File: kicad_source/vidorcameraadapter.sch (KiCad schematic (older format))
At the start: 44 parts, among them CN1 CONN_02X26, CN2 CONN_02X10, CN3 CONN_01X03

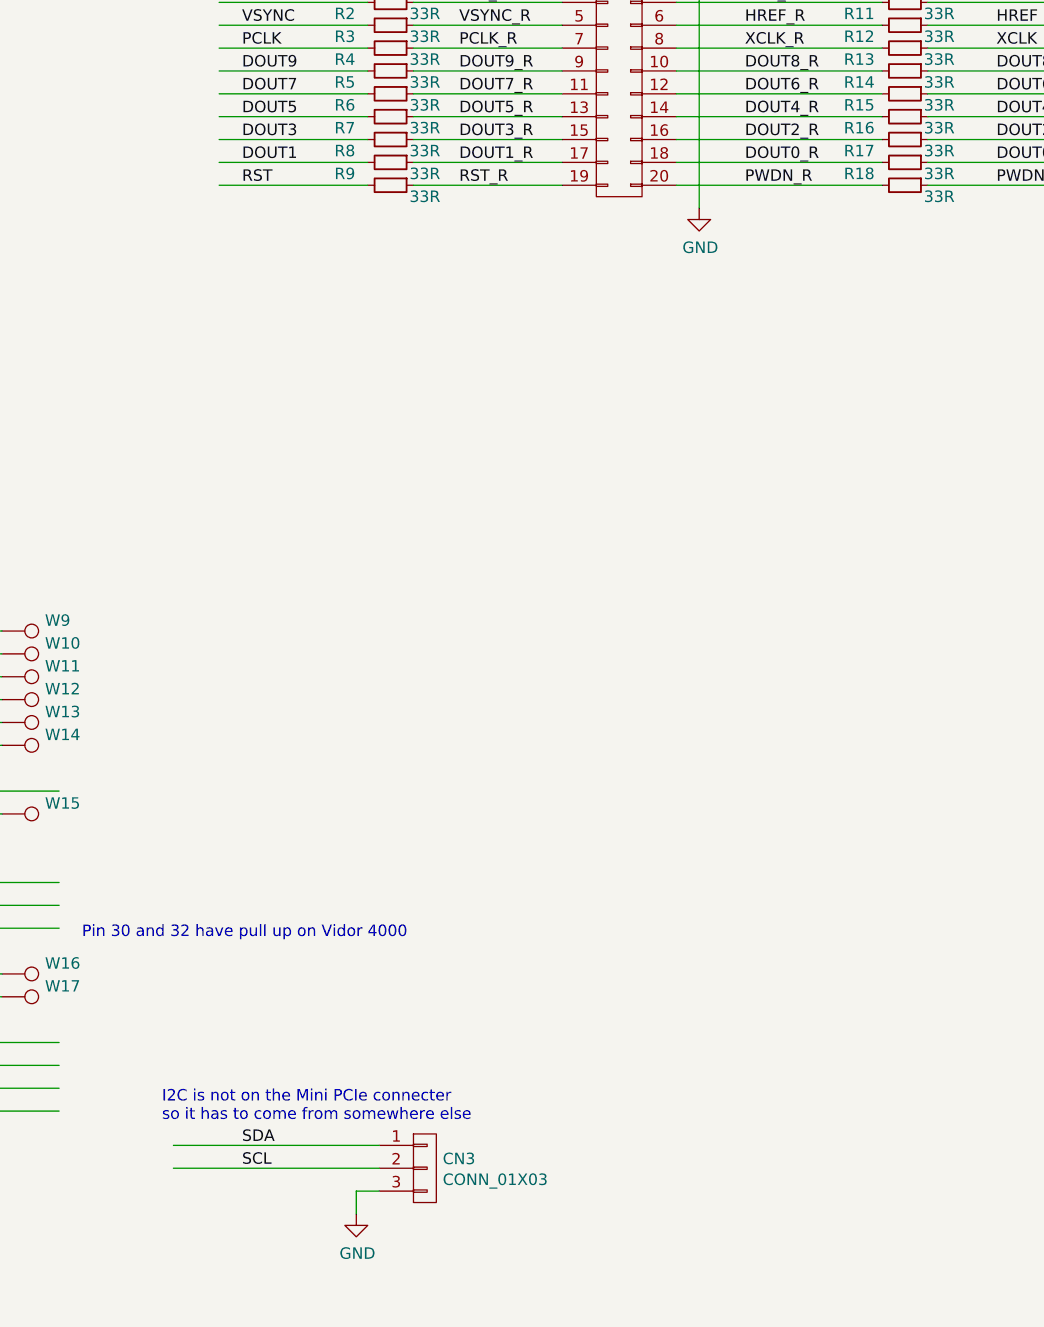
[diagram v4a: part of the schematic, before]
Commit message: added pull up for I2C and RST, added pull down for pwdn
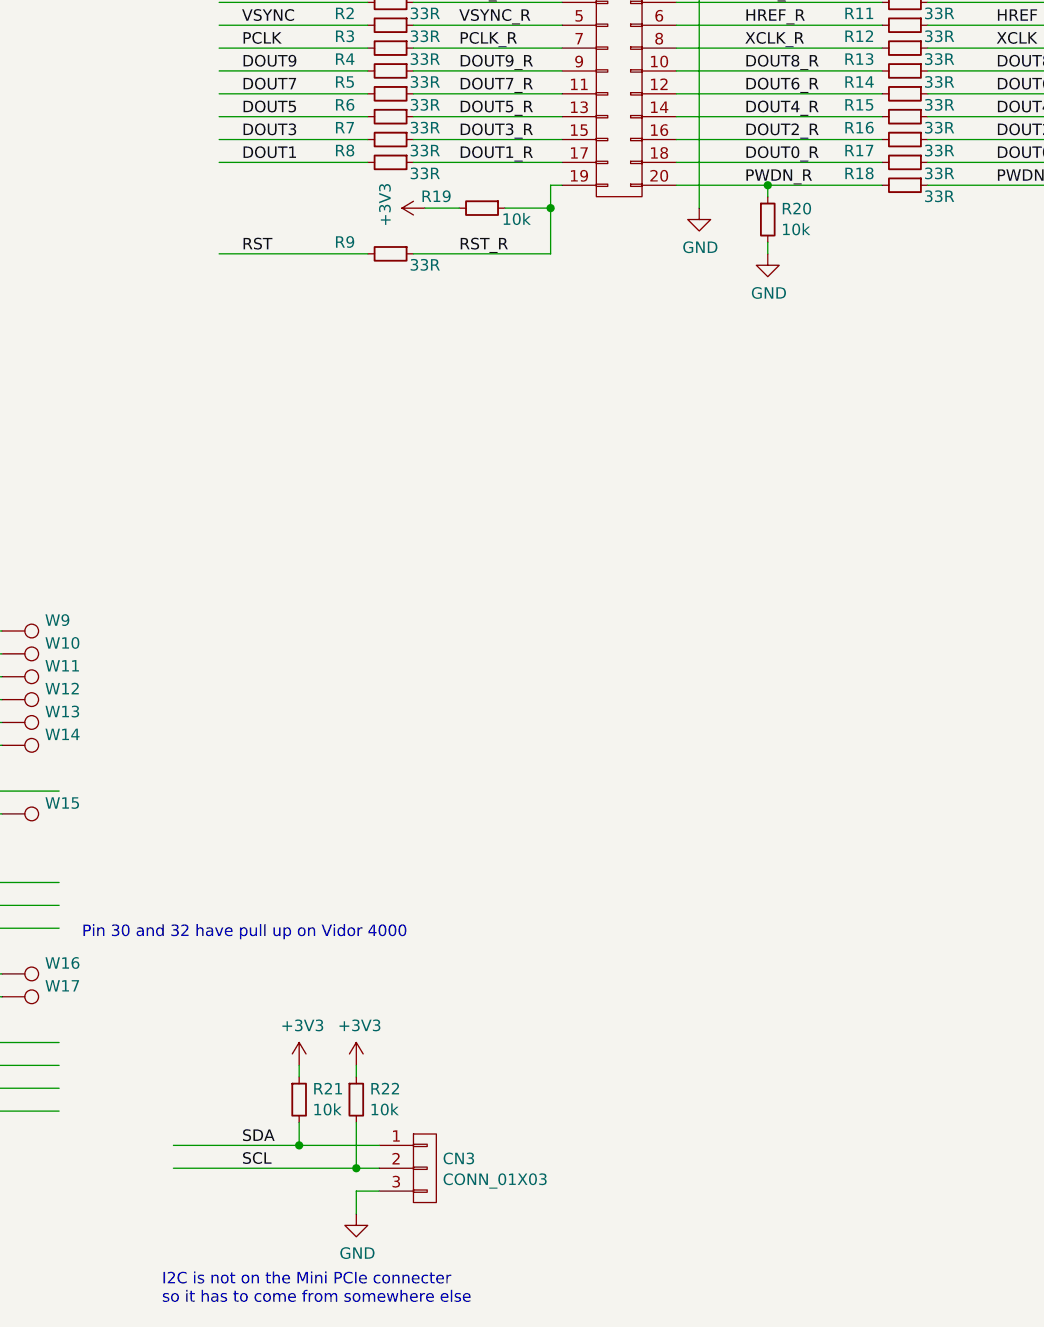
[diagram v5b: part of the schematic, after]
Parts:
- added R19, R20, R21, R22: 10k, resistors:R_0603, symbol devices:R_0603
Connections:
- wire segments 115 -> 129
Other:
- moved on the sheet: R9
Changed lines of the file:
@@
 	6300 2350 6950 2350
 Wire Wire Line
-	6300 2450 6950 2450
-Wire Wire Line
 	8350 1650 7450 1650
 Wire Wire Line
@@
 	8350 2350 7450 2350
 Wire Wire Line
-	8350 2450 7450 2450
+	8350 2450 7850 2450
 Text Label 6500 1650 0    50   ~ 0
 SCL_R
@@
 Text Label 7750 1850 0    50   ~ 0
 XCLK_R
-Text Label 6500 2450 0    50   ~ 0
+Text Label 6500 2750 0    50   ~ 0
 RST_R
 Text Label 7750 2450 0    50   ~ 0
@@
 DOUT1
 Wire Wire Line
-	6150 6650 5250 6650
-Wire Wire Line
-	6150 6750 5250 6750
+	6150 6650 5800 6650
+Wire Wire Line
+	6150 6750 6050 6750
 Text Label 5550 6650 0    50   ~ 0
 SDA
@@
 Wire Wire Line
 	6050 6850 6050 6950
-Text Notes 5200 6550 0    50   ~ 0
+Text Notes 5200 7350 0    50   ~ 0
 I2C is not on the Mini PCIe connecter\nso it has to come from somewhere else
 $Comp
@@
 Wire Wire Line
 	5450 2350 6100 2350
-Wire Wire Line
-	5450 2450 6100 2450
 Text Label 5550 1650 0    50   ~ 0
 SCL
@@
 Text Label 5550 1850 0    50   ~ 0
 PCLK
-Text Label 5550 2450 0    50   ~ 0
+Text Label 5550 2750 0    50   ~ 0
 RST
 Text Label 5550 1950 0    50   ~ 0
@@
 L devices:R_0603 R9
 U 1 1 5E32ABC3
-P 6200 2450
-F 0 "R9" V 6150 2250 50  0000 C CNN
-F 1 "33R" V 6250 2600 50  0000 C CNN
-F 2 "resistors:R_0603" H 6200 2300 50  0001 C CNN
-F 3 "" H 6200 2450 50  0000 C CNN
-	1    6200 2450
+P 6200 2750
+F 0 "R9" V 6150 2550 50  0000 C CNN
+F 1 "33R" V 6250 2900 50  0000 C CNN
+F 2 "resistors:R_0603" H 6200 2600 50  0001 C CNN
+F 3 "" H 6200 2750 50  0000 C CNN
+	1    6200 2750
 	0    1    1    0
 $EndComp
@@
 	0    -1   -1   0
 $EndComp
+Wire Wire Line
+	5450 2750 6100 2750
+Wire Wire Line
+	6300 2750 6900 2750
+Wire Wire Line
+	6900 2750 6900 2550
+Wire Wire Line
+	6900 2450 6950 2450
+$Comp
+L devices:R_0603 R19
+U 1 1 5E34B16D
+P 6600 2550
+F 0 "R19" V 6550 2350 50  0000 C CNN
+F 1 "10k" V 6650 2700 50  0000 C CNN
+F 2 "resistors:R_0603" H 6600 2400 50  0001 C CNN
+F 3 "" H 6600 2550 50  0000 C CNN
+	1    6600 2550
+	0    1    1    0
+$EndComp
+$Comp
+L power-supply:+3V3 #PWR02
+U 1 1 5E34B540
+P 6350 2550
+F 0 "#PWR02" H 6350 2400 50  0001 C CNN
+F 1 "+3V3" H 6365 2723 50  0000 C CNN
+F 2 "" H 6350 2550 50  0000 C CNN
+F 3 "" H 6350 2550 50  0000 C CNN
+	1    6350 2550
+	0    -1   -1   0
+$EndComp
+Wire Wire Line
+	6350 2550 6500 2550
+Wire Wire Line
+	6700 2550 6900 2550
+Connection ~ 6900 2550
+Wire Wire Line
+	6900 2550 6900 2450
+$Comp
+L devices:R_0603 R20
+U 1 1 5E358A18
+P 7850 2600
+F 0 "R20" H 7909 2646 50  0000 L CNN
+F 1 "10k" H 7909 2555 50  0000 L CNN
+F 2 "resistors:R_0603" H 7850 2450 50  0001 C CNN
+F 3 "" H 7850 2600 50  0000 C CNN
+	1    7850 2600
+	1    0    0    -1
+$EndComp
+$Comp
+L power-supply:GND #PWR03
+U 1 1 5E359892
+P 7850 2750
+F 0 "#PWR03" H 7850 2500 50  0001 C CNN
+F 1 "GND" H 7855 2577 50  0000 C CNN
+F 2 "" H 7850 2750 50  0000 C CNN
+F 3 "" H 7850 2750 50  0000 C CNN
+	1    7850 2750
+	1    0    0    -1
+$EndComp
+Wire Wire Line
+	7850 2500 7850 2450
+Connection ~ 7850 2450
+Wire Wire Line
+	7850 2450 7450 2450
+Wire Wire Line
+	7850 2700 7850 2750
+$Comp
+L devices:R_0603 R21
+U 1 1 5E3698B8
+P 5800 6450
+F 0 "R21" H 5859 6496 50  0000 L CNN
+F 1 "10k" H 5859 6405 50  0000 L CNN
+F 2 "resistors:R_0603" H 5800 6300 50  0001 C CNN
+F 3 "" H 5800 6450 50  0000 C CNN
+	1    5800 6450
+	1    0    0    -1
+$EndComp
+$Comp
+L devices:R_0603 R22
+U 1 1 5E36B62F
+P 6050 6450
+F 0 "R22" H 6109 6496 50  0000 L CNN
+F 1 "10k" H 6109 6405 50  0000 L CNN
+F 2 "resistors:R_0603" H 6050 6300 50  0001 C CNN
+F 3 "" H 6050 6450 50  0000 C CNN
+	1    6050 6450
+	1    0    0    -1
+$EndComp
+$Comp
+L power-supply:+3V3 #PWR04
+U 1 1 5E36D8CA
+P 5800 6300
+F 0 "#PWR04" H 5800 6150 50  0001 C CNN
+F 1 "+3V3" H 5815 6473 50  0000 C CNN
+F 2 "" H 5800 6300 50  0000 C CNN
+F 3 "" H 5800 6300 50  0000 C CNN
+	1    5800 6300
+	1    0    0    -1
+$EndComp
+$Comp
+L power-supply:+3V3 #PWR05
+U 1 1 5E370008
+P 6050 6300
+F 0 "#PWR05" H 6050 6150 50  0001 C CNN
+F 1 "+3V3" H 6065 6473 50  0000 C CNN
+F 2 "" H 6050 6300 50  0000 C CNN
+F 3 "" H 6050 6300 50  0000 C CNN
+	1    6050 6300
+	1    0    0    -1
+$EndComp
+Wire Wire Line
+	5800 6550 5800 6650
+Connection ~ 5800 6650
+Wire Wire Line
+	5800 6650 5250 6650
+Wire Wire Line
+	6050 6550 6050 6750
+Connection ~ 6050 6750
+Wire Wire Line
+	6050 6750 5250 6750
+Wire Wire Line
+	6050 6350 6050 6300
+Wire Wire Line
+	5800 6350 5800 6300
 $EndSCHEMATC

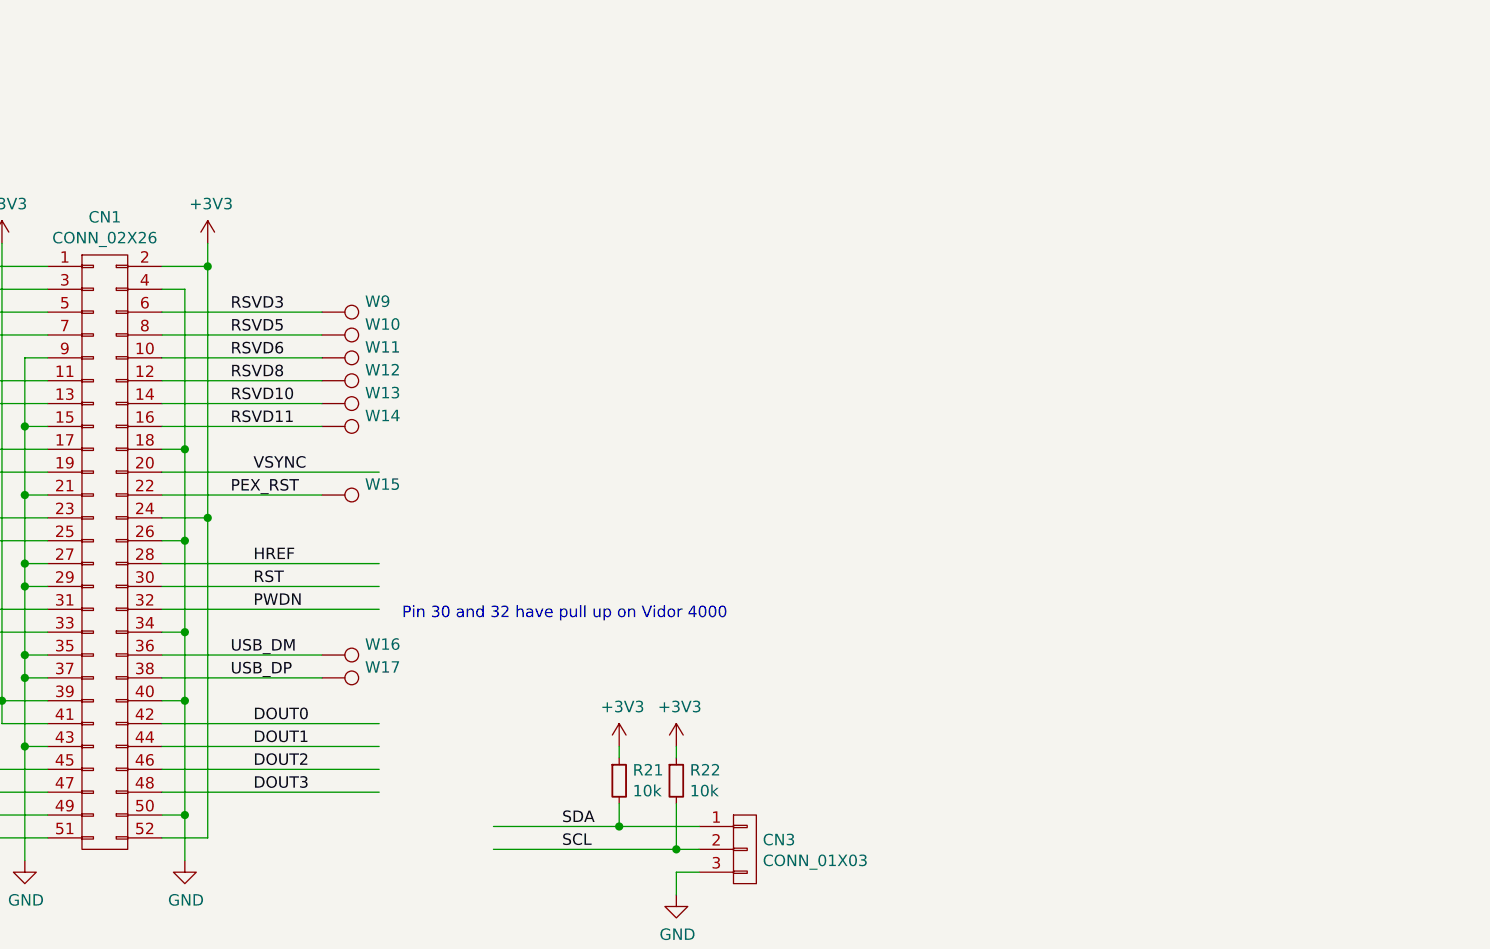
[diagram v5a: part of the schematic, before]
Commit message: connected I2C to Vidor 4000, added LEDs
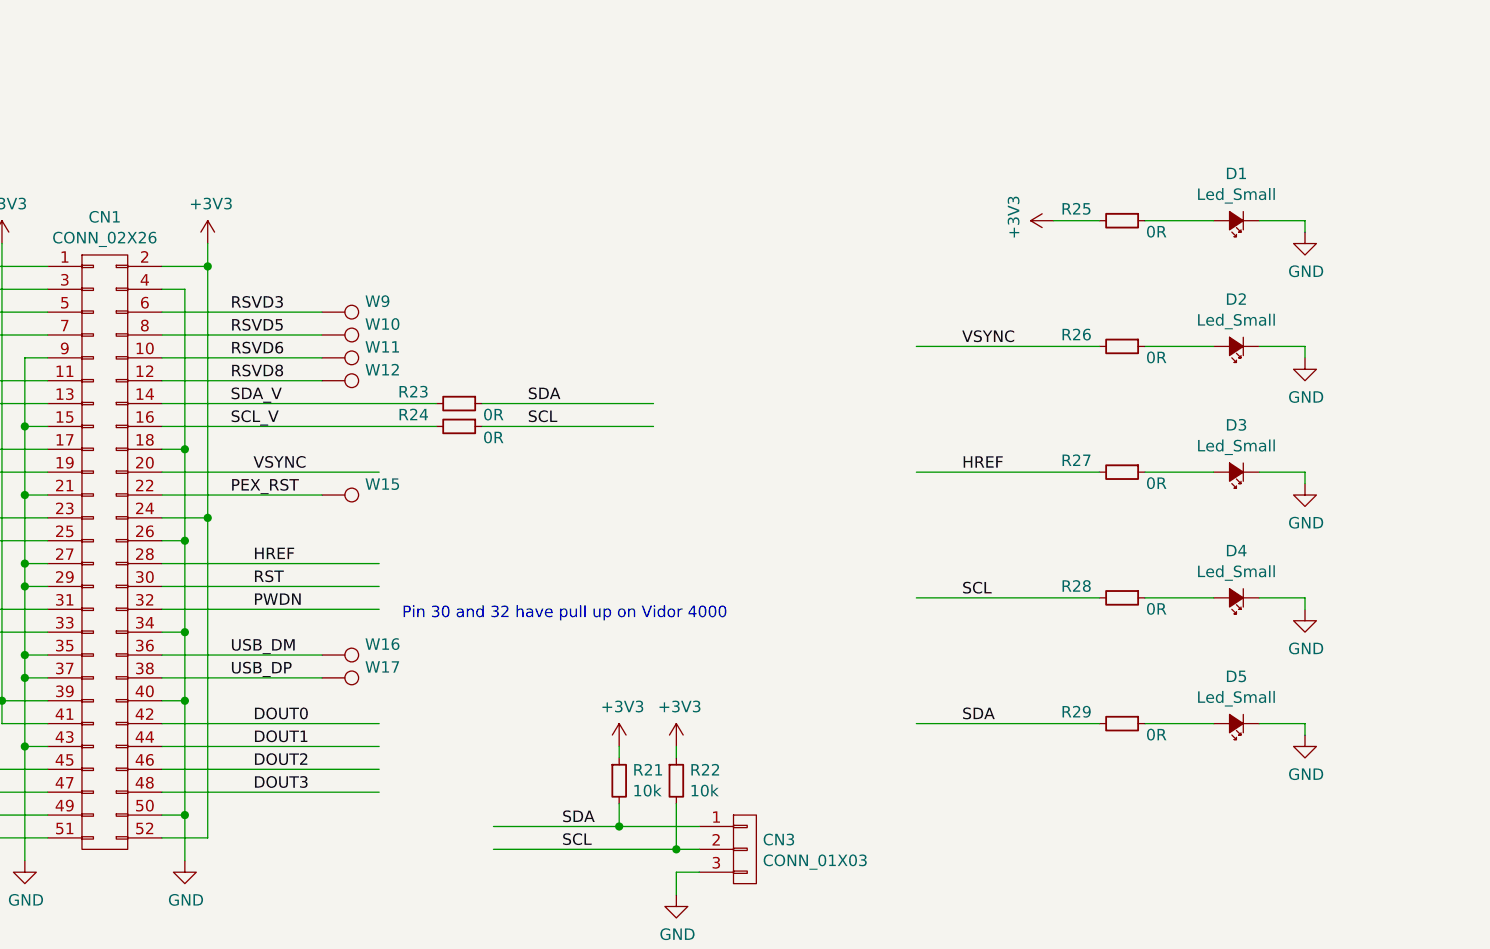
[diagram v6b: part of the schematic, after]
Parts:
- removed W13, W14: TEST_1P, wire_pads:SolderWirePad_single_1mmSMD, symbol mechanical-connectors:TEST_1P
- added D1, D2, D3, D4, D5: Led_Small, symbol devices:Led_Small
- added R23, R24, R25, R26, R27, R28, R29: 0R, resistors:R_0603, symbol devices:R_0603
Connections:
- net labels added: SCL_V, SDA_V
- net labels removed: RSVD10, RSVD11
- wire segments 129 -> 151

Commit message: added RGB led
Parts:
- removed W6, W7, W8: TEST_1P, wire_pads:SolderWirePad_single_1mmSMD, symbol mechanical-connectors:TEST_1P
- added D6: LED_RABG, symbol devices:LED_RABG
- added R30, R31, R32: 1k, resistors:R_0603, symbol devices:R_0603
- R25, R26, R27, R28, R29: value 0R -> 1k
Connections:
- net labels added: LED_B, LED_G, LED_R
- net labels removed: RSVD12, RSVD13, RSVD9
- wire segments 151 -> 159
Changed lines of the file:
@@
 	2650 4700 3300 4700
-Wire Wire Line
-	2650 4800 3300 4800
-Wire Wire Line
-	2650 5000 3300 5000
-Wire Wire Line
-	2650 5100 3300 5100
 Wire Wire Line
 	4500 4700 3800 4700
@@
 Text Label 4100 4700 0    50   ~ 0
 RSVD8
-Text Label 2750 4800 0    50   ~ 0
-RSVD9
+Text Label 2550 4800 0    50   ~ 0
+LED_R
 Text Label 4100 4800 0    50   ~ 0
 SDA_V
 Text Label 4100 4900 0    50   ~ 0
 SCL_V
-Text Label 2750 5000 0    50   ~ 0
-RSVD12
-Text Label 2750 5100 0    50   ~ 0
-RSVD13
+Text Label 2550 5000 0    50   ~ 0
+LED_G
+Text Label 2550 5100 0    50   ~ 0
+LED_B
 $Comp
 L MECH_smd-spacer:WA-SMSI_9774015151 MECH1
@@
 $EndComp
 $Comp
-L mechanical-connectors:TEST_1P W8
-U 1 1 5E317186
-P 2650 5100
-F 0 "W8" V 2650 5350 50  0000 C CNN
-F 1 "TEST_1P" V 2754 5172 50  0001 C CNN
-F 2 "wire_pads:SolderWirePad_single_1mmSMD" V 2741 5288 50  0001 L CNN
-F 3 "" H 2850 5100 50  0000 C CNN
-	1    2650 5100
-	0    -1   -1   0
-$EndComp
-$Comp
-L mechanical-connectors:TEST_1P W7
-U 1 1 5E31844B
-P 2650 5000
-F 0 "W7" V 2650 5250 50  0000 C CNN
-F 1 "TEST_1P" V 2754 5072 50  0001 C CNN
-F 2 "wire_pads:SolderWirePad_single_1mmSMD" V 2741 5188 50  0001 L CNN
-F 3 "" H 2850 5000 50  0000 C CNN
-	1    2650 5000
-	0    -1   -1   0
-$EndComp
-$Comp
-L mechanical-connectors:TEST_1P W6
-U 1 1 5E318681
-P 2650 4800
-F 0 "W6" V 2650 5050 50  0000 C CNN
-F 1 "TEST_1P" V 2754 4872 50  0001 C CNN
-F 2 "wire_pads:SolderWirePad_single_1mmSMD" V 2741 4988 50  0001 L CNN
-F 3 "" H 2850 4800 50  0000 C CNN
-	1    2650 4800
-	0    -1   -1   0
-$EndComp
-$Comp
 L mechanical-connectors:TEST_1P W5
 U 1 1 5E31885D
@@
 P 8000 6200
 F 0 "R29" V 7950 6000 50  0000 C CNN
-F 1 "0R" V 8050 6350 50  0000 C CNN
+F 1 "1k" V 8050 6350 50  0000 C CNN
 F 2 "resistors:R_0603" H 8000 6050 50  0001 C CNN
 F 3 "" H 8000 6200 50  0000 C CNN
@@
 P 8000 5650
 F 0 "R28" V 7950 5450 50  0000 C CNN
-F 1 "0R" V 8050 5800 50  0000 C CNN
+F 1 "1k" V 8050 5800 50  0000 C CNN
 F 2 "resistors:R_0603" H 8000 5500 50  0001 C CNN
 F 3 "" H 8000 5650 50  0000 C CNN
@@
 P 8000 5100
 F 0 "R27" V 7950 4900 50  0000 C CNN
-F 1 "0R" V 8050 5250 50  0000 C CNN
+F 1 "1k" V 8050 5250 50  0000 C CNN
 F 2 "resistors:R_0603" H 8000 4950 50  0001 C CNN
 F 3 "" H 8000 5100 50  0000 C CNN
@@
 P 8000 4550
 F 0 "R26" V 7950 4350 50  0000 C CNN
-F 1 "0R" V 8050 4700 50  0000 C CNN
+F 1 "1k" V 8050 4700 50  0000 C CNN
 F 2 "resistors:R_0603" H 8000 4400 50  0001 C CNN
 F 3 "" H 8000 4550 50  0000 C CNN
@@
 P 8000 4000
 F 0 "R25" V 7950 3800 50  0000 C CNN
-F 1 "0R" V 8050 4150 50  0000 C CNN
+F 1 "1k" V 8050 4150 50  0000 C CNN
 F 2 "resistors:R_0603" H 8000 3850 50  0001 C CNN
 F 3 "" H 8000 4000 50  0000 C CNN
@@
 Wire Wire Line
 	7900 4000 7700 4000
+$Comp
+L devices:LED_RABG D6
+U 1 1 5E3EF9EF
+P 10500 5750
+F 0 "D6" H 10500 6215 50  0000 C CNN
+F 1 "LED_RABG" H 10500 6124 50  0000 C CNN
+F 2 "" H 10450 5700 50  0000 C CNN
+F 3 "" H 10450 5700 50  0000 C CNN
+	1    10500 5750
+	1    0    0    -1
+$EndComp
+$Comp
+L devices:R_0603 R32
+U 1 1 5E3F2B43
+P 9950 5950
+F 0 "R32" V 9900 5750 50  0000 C CNN
+F 1 "1k" V 10000 6100 50  0000 C CNN
+F 2 "resistors:R_0603" H 9950 5800 50  0001 C CNN
+F 3 "" H 9950 5950 50  0000 C CNN
+	1    9950 5950
+	0    1    1    0
+$EndComp
+$Comp
+L devices:R_0603 R31
+U 1 1 5E3F3138
+P 9950 5750
+F 0 "R31" V 9900 5550 50  0000 C CNN
+F 1 "1k" V 10000 5900 50  0000 C CNN
+F 2 "resistors:R_0603" H 9950 5600 50  0001 C CNN
+F 3 "" H 9950 5750 50  0000 C CNN
+	1    9950 5750
+	0    1    1    0
+$EndComp
+$Comp
+L devices:R_0603 R30
+U 1 1 5E3F33D7
+P 9950 5550
+F 0 "R30" V 9900 5350 50  0000 C CNN
+F 1 "1k" V 10000 5700 50  0000 C CNN
+F 2 "resistors:R_0603" H 9950 5400 50  0001 C CNN
+F 3 "" H 9950 5550 50  0000 C CNN
+	1    9950 5550
+	0    1    1    0
+$EndComp
+$Comp
+L power-supply:+3V3 #PWR012
+U 1 1 5E3F36D6
+P 10950 5650
+F 0 "#PWR012" H 10950 5500 50  0001 C CNN
+F 1 "+3V3" H 10965 5823 50  0000 C CNN
+F 2 "" H 10950 5650 50  0000 C CNN
+F 3 "" H 10950 5650 50  0000 C CNN
+	1    10950 5650
+	1    0    0    -1
+$EndComp
+Wire Wire Line
+	9050 5550 9850 5550
+Wire Wire Line
+	9050 5750 9850 5750
+Wire Wire Line
+	9050 5950 9850 5950
+Wire Wire Line
+	10050 5950 10200 5950
+Wire Wire Line
+	10200 5750 10050 5750
+Wire Wire Line
+	10050 5550 10200 5550
+Wire Wire Line
+	10800 5750 10950 5750
+Wire Wire Line
+	10950 5750 10950 5650
+Text Label 9100 5550 0    50   ~ 0
+LED_R
+Text Label 9100 5750 0    50   ~ 0
+LED_G
+Text Label 9100 5950 0    50   ~ 0
+LED_B
+Wire Wire Line
+	2450 5100 3300 5100
+Wire Wire Line
+	2450 5000 3300 5000
+Wire Wire Line
+	2450 4800 3300 4800
 $EndSCHEMATC
